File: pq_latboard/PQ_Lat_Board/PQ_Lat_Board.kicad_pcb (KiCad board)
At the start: 6 copper layers, 48 x 48 mm, 20 parts, among them IC1 TCN75AVOA713, J1 Conn_01x11_MountingPin, J2 connector-coax

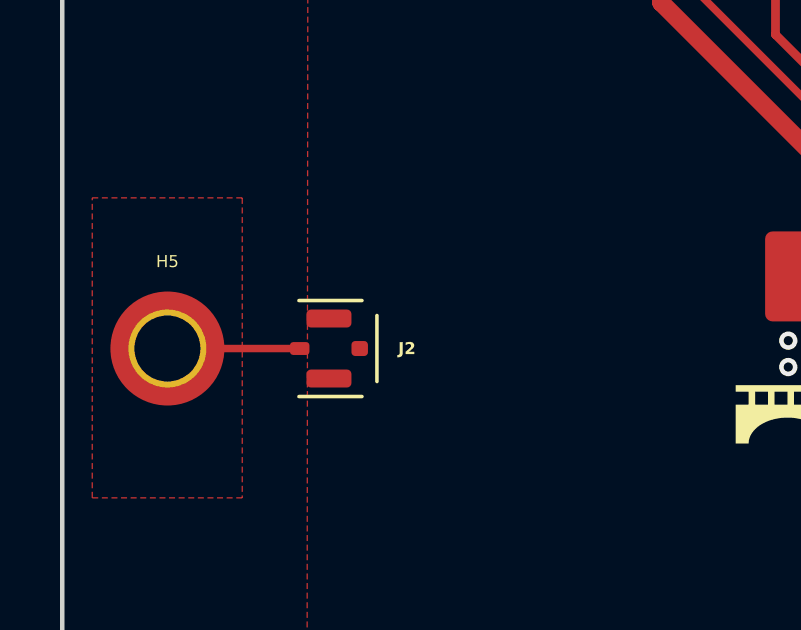
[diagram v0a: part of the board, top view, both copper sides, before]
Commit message: solved wrong connector in lateral board
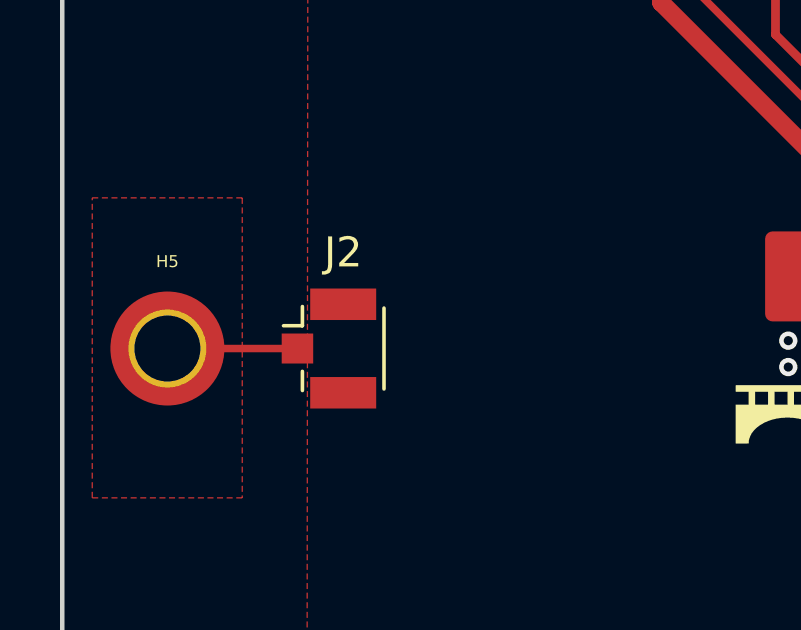
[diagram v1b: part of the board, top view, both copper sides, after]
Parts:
- J2: value connector-coax -> Conn_Coaxial; footprint -nsl_connector:C.FL-R-SMT-1(90) -> Connector_Coaxial:U.FL_Hirose_U.FL-R-SMT-1_Vertical
- turned J2 to 0 degrees
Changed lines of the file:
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@@
       (net 8 "/Antenna Connector") (pinfunction "1") (pintype "input"))
   )
-  (footprint "-nsl_connector:C.FL-R-SMT-1(90)" (layer "F.Cu")
-    (at 83.89 66.0224 -90)
-    (property "Manufacturer 1" "Hirose")
-    (property "Manufacturer Part Number 1" "C.FL-R-SMT-1")
+  (footprint "Connector_Coaxial:U.FL_Hirose_U.FL-R-SMT-1_Vertical" (layer "F.Cu")
+    (at 83.89 66.0224)
+    (descr "Hirose U.FL Coaxial https://www.hirose.com/product/en/products/U.FL/U.FL-R-SMT-1%2810%29/")
+    (tags "Hirose U.FL Coaxial")
     (property "Sheetfile" "PQ_Lat_Board.kicad_sch")
     (property "Sheetname" "")
-    (property "Supplier 1" "Mouser")
-    (property "Supplier Part Number 1" "798-CFL-R-SMT-190 ")
+    (property "ki_description" "coaxial connector (BNC, SMA, SMB, SMC, Cinch/RCA, LEMO, ...)")
+    (property "ki_keywords" "BNC SMA SMB SMC LEMO coaxial connector CINCH RCA")
     (attr smd)
-    (fp_text reference "J2" (at 0 -2.6 unlocked) (layer "F.SilkS")
-        (effects (font (size 0.4 0.4) (thickness 0.1) bold))
-    )
-    (fp_text value "connector-coax" (at 0 -5.4 -90 unlocked) (layer "F.Fab")
+    (fp_text reference "J2" (at 0.475 -3.2) (layer "F.SilkS")
         (effects (font (size 1 1) (thickness 0.15)))
     )
-    (fp_text user "${REFERENCE}" (at 0 -3.9 -90 unlocked) (layer "F.Fab")
+    (fp_text value "Conn_Coaxial" (at 0.475 3.2) (layer "F.Fab")
         (effects (font (size 1 1) (thickness 0.15)))
     )
-    (fp_line (start -1.6 1) (end -1.6 -1.1)
+    (fp_text user "${REFERENCE}" (at 0.475 0 90) (layer "F.Fab")
+        (effects (font (size 0.6 0.6) (thickness 0.09)))
+    )
+    (fp_line (start -0.885 -1.4) (end -0.885 -0.76)
       (stroke (width 0.12) (type solid)) (layer "F.SilkS"))
-    (fp_line (start -1.1 -1.6) (end 1.1 -1.6)
+    (fp_line (start -0.885 -0.76) (end -1.515 -0.76)
       (stroke (width 0.12) (type solid)) (layer "F.SilkS"))
-    (fp_line (start 1.6 -1.1) (end 1.6 1)
+    (fp_line (start -0.885 1.4) (end -0.885 0.76)
       (stroke (width 0.12) (type solid)) (layer "F.SilkS"))
-    (pad "1" smd roundrect (at 0 0.975 90) (size 0.43 0.65) (layers "F.Cu" "F.Paste" "F.Mask") (roundrect_rratio 0.25)
-      (net 8 "/Antenna Connector") (pintype "bidirectional"))
-    (pad "2" smd roundrect (at -1 0 90) (size 0.6 1.5) (layers "F.Cu" "F.Paste" "F.Mask") (roundrect_rratio 0.25)
-      (net 9 "GND") (pintype "bidirectional"))
-    (pad "2" smd roundrect (at 0 -1.025 90) (size 0.5 0.55) (layers "F.Cu" "F.Paste" "F.Mask") (roundrect_rratio 0.25)
-      (net 9 "GND") (pintype "bidirectional"))
-    (pad "2" smd roundrect (at 1 0 90) (size 0.6 1.5) (layers "F.Cu" "F.Paste" "F.Mask") (roundrect_rratio 0.25)
-      (net 9 "GND") (pintype "bidirectional"))
-    (model "${KICAD_NSL_DIR}/connector-nsl/StepFiles/C.FL-R-SMT-1(90).stp"
-      (offset (xyz 0 0 0))
+    (fp_line (start 1.835 -1.35) (end 1.835 1.35)
+      (stroke (width 0.12) (type solid)) (layer "F.SilkS"))
+    (fp_line (start -2.02 1) (end -2.02 -1)
+      (stroke (width 0.05) (type solid)) (layer "F.CrtYd"))
+    (fp_line (start -1.32 -1.8) (end -1.12 -1.8)
+      (stroke (width 0.05) (type solid)) (layer "F.CrtYd"))
+    (fp_line (start -1.32 -1) (end -2.02 -1)
+      (stroke (width 0.05) (type solid)) (layer "F.CrtYd"))
+    (fp_line (start -1.32 -1) (end -1.32 -1.8)
+      (stroke (width 0.05) (type solid)) (layer "F.CrtYd"))
+    (fp_line (start -1.32 1) (end -2.02 1)
+      (stroke (width 0.05) (type solid)) (layer "F.CrtYd"))
+    (fp_line (start -1.32 1.8) (end -1.32 1)
+      (stroke (width 0.05) (type solid)) (layer "F.CrtYd"))
+    (fp_line (start -1.32 1.8) (end -1.12 1.8)
+      (stroke (width 0.05) (type solid)) (layer "F.CrtYd"))
+    (fp_line (start -1.12 -1.8) (end -1.12 -2.5)
+      (stroke (width 0.05) (type solid)) (layer "F.CrtYd"))
+    (fp_line (start -1.12 2.5) (end -1.12 1.8)
+      (stroke (width 0.05) (type solid)) (layer "F.CrtYd"))
+    (fp_line (start 2.08 -2.5) (end -1.12 -2.5)
+      (stroke (width 0.05) (type solid)) (layer "F.CrtYd"))
+    (fp_line (start 2.08 -1.8) (end 2.08 -2.5)
+      (stroke (width 0.05) (type solid)) (layer "F.CrtYd"))
+    (fp_line (start 2.08 -1.8) (end 2.28 -1.8)
+      (stroke (width 0.05) (type solid)) (layer "F.CrtYd"))
+    (fp_line (start 2.08 1.8) (end 2.28 1.8)
+      (stroke (width 0.05) (type solid)) (layer "F.CrtYd"))
+    (fp_line (start 2.08 2.5) (end -1.12 2.5)
+      (stroke (width 0.05) (type solid)) (layer "F.CrtYd"))
+    (fp_line (start 2.08 2.5) (end 2.08 1.8)
+      (stroke (width 0.05) (type solid)) (layer "F.CrtYd"))
+    (fp_line (start 2.28 1.8) (end 2.28 -1.8)
+      (stroke (width 0.05) (type solid)) (layer "F.CrtYd"))
+    (fp_line (start -1.075 0.3) (end -1.075 -0.15)
+      (stroke (width 0.1) (type solid)) (layer "F.Fab"))
+    (fp_line (start -1.075 0.3) (end -0.825 0.3)
+      (stroke (width 0.1) (type solid)) (layer "F.Fab"))
+    (fp_line (start -0.925 -0.3) (end -1.075 -0.15)
+      (stroke (width 0.1) (type solid)) (layer "F.Fab"))
+    (fp_line (start -0.925 -0.3) (end -0.825 -0.3)
+      (stroke (width 0.1) (type solid)) (layer "F.Fab"))
+    (fp_line (start -0.825 -0.3) (end -0.825 -1.3)
+      (stroke (width 0.1) (type solid)) (layer "F.Fab"))
+    (fp_line (start -0.825 0.3) (end -0.825 1.3)
+      (stroke (width 0.1) (type solid)) (layer "F.Fab"))
+    (fp_line (start -0.425 -1.5) (end -0.425 -1.3)
+      (stroke (width 0.1) (type solid)) (layer "F.Fab"))
+    (fp_line (start -0.425 -1.5) (end 1.375 -1.5)
+      (stroke (width 0.1) (type solid)) (layer "F.Fab"))
+    (fp_line (start -0.425 -1.3) (end -0.825 -1.3)
+      (stroke (width 0.1) (type solid)) (layer "F.Fab"))
+    (fp_line (start -0.425 1.3) (end -0.825 1.3)
+      (stroke (width 0.1) (type solid)) (layer "F.Fab"))
+    (fp_line (start -0.425 1.5) (end -0.425 1.3)
+      (stroke (width 0.1) (type solid)) (layer "F.Fab"))
+    (fp_line (start -0.425 1.5) (end 1.375 1.5)
+      (stroke (width 0.1) (type solid)) (layer "F.Fab"))
+    (fp_line (start 1.375 -1.5) (end 1.375 -1.3)
+      (stroke (width 0.1) (type solid)) (layer "F.Fab"))
+    (fp_line (start 1.375 1.5) (end 1.375 1.3)
+      (stroke (width 0.1) (type solid)) (layer "F.Fab"))
+    (fp_line (start 1.775 -1.3) (end 1.375 -1.3)
+      (stroke (width 0.1) (type solid)) (layer "F.Fab"))
+    (fp_line (start 1.775 -1.3) (end 1.775 1.3)
+      (stroke (width 0.1) (type solid)) (layer "F.Fab"))
+    (fp_line (start 1.775 1.3) (end 1.375 1.3)
+      (stroke (width 0.1) (type solid)) (layer "F.Fab"))
+    (pad "1" smd rect (at -1.05 0) (size 1.05 1) (layers "F.Cu" "F.Paste" "F.Mask")
+      (net 8 "/Antenna Connector") (pinfunction "In") (pintype "passive"))
+    (pad "2" smd rect (at 0.475 -1.475) (size 2.2 1.05) (layers "F.Cu" "F.Paste" "F.Mask")
+      (net 9 "GND") (pinfunction "Ext") (pintype "passive"))
+    (pad "2" smd rect (at 0.475 1.475) (size 2.2 1.05) (layers "F.Cu" "F.Paste" "F.Mask")
+      (net 9 "GND") (pinfunction "Ext") (pintype "passive"))
+    (model "${KICAD6_3DMODEL_DIR}/Connector_Coaxial.3dshapes/U.FL_Hirose_U.FL-R-SMT-1_Vertical.wrl"
+      (offset (xyz 0.4749999928 0 0))
       (scale (xyz 1 1 1))
       (rotate (xyz 0 0 0))

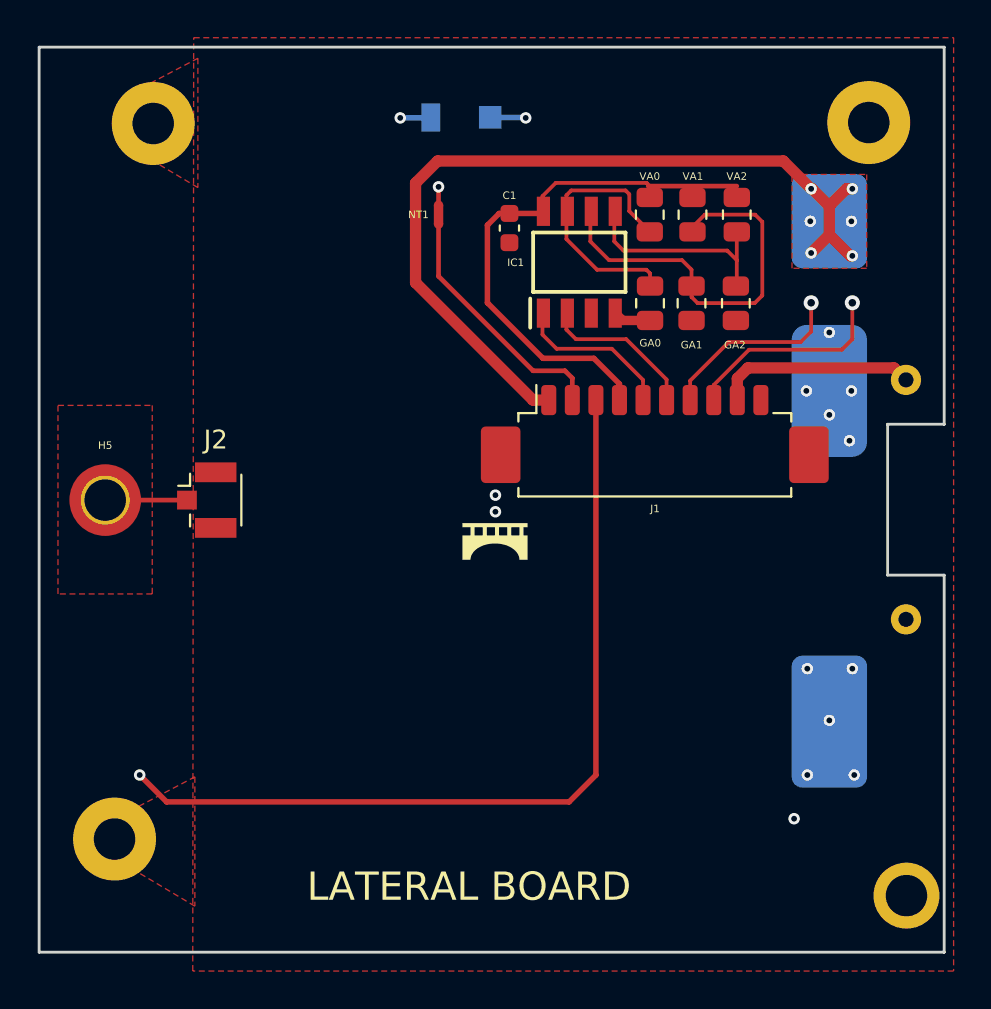
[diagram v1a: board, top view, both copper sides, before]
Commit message: add names, bigger hole and mirror solar cell
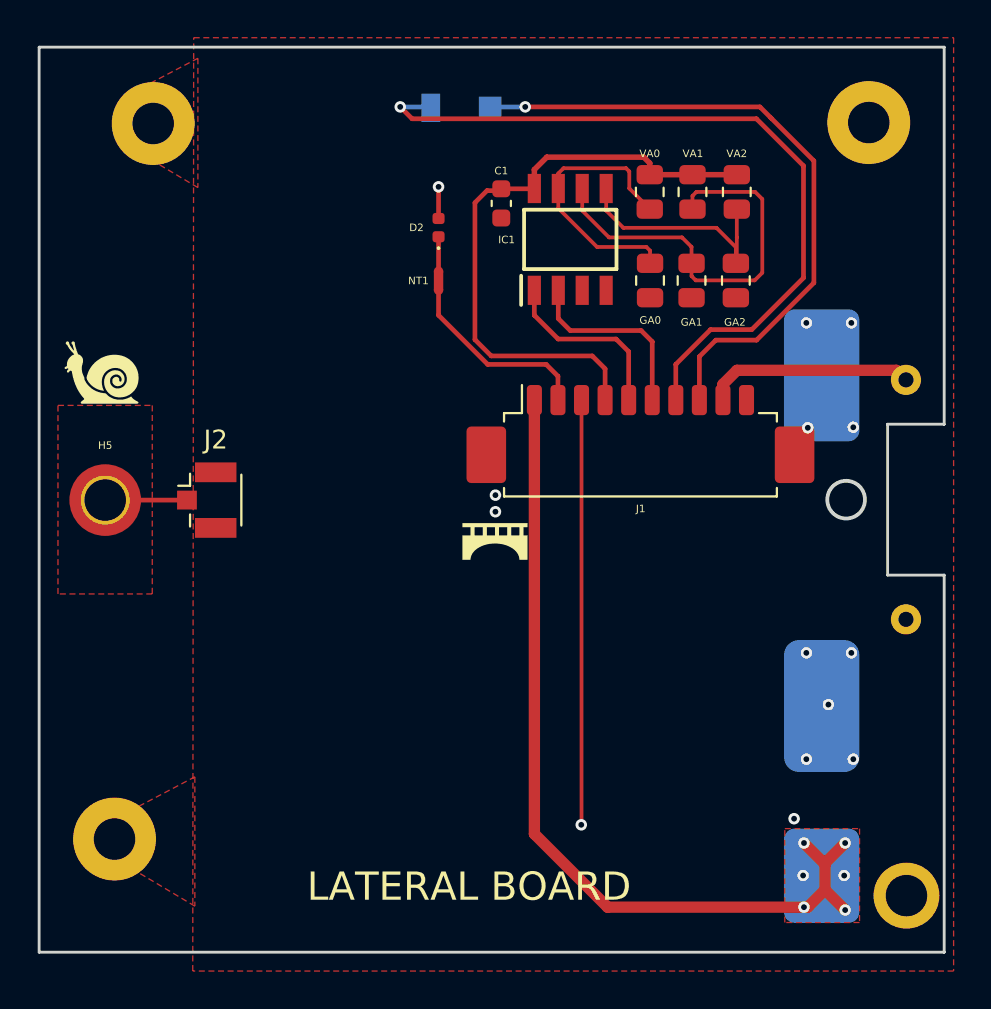
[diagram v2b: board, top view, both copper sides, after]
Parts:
- added Annotation2: Silkscreen_Annotation, symbols-nsl:snail, F.Cu at (78.3, 59.3)
- added Annotation3: LOGO, symbols-nsl:pocat-lektron, B.Cu at (108.9, 45.1)
- added Annotation4: Logo lektron, symbols-nsl:logo_pq, B.Cu at (78.8, 57.0)
- added Annotation5: telecos, symbols-nsl:Telecos, B.Cu at (88.5, 45.3)
- added Annotation6: telecos, symbols-nsl:NSL-small, B.Cu at (76.9, 75.0)
- added Annotation7: IEEE, symbols-nsl:UPC_small, B.Cu at (80.3, 72.9)
- added Annotation8: GRSS, symbols-nsl:GRSS, B.Cu at (118.3, 52.1)
- added D2: LED, LED_SMD:LED_0402_1005Metric, F.Cu at (96.2, 51.6)
- moved NT1 3.51 mm to (96.2, 54.4)
- moved C1 1.38 mm to (99.5, 50.3)
- moved IC1 1.30 mm to (103.1, 52.2)
- moved VA0 1.21 mm to (107.4, 49.7)
- moved VA1 1.21 mm to (109.7, 49.7)
- moved VA2 1.21 mm to (112.0, 49.7)
- moved GA0 1.21 mm to (107.4, 54.4)
- moved GA1 1.21 mm to (109.6, 54.4)
- moved GA2 1.21 mm to (112.0, 54.4)
- moved J1 0.76 mm to (106.9, 63.1)
- moved D1 0.51 mm to (97.7, 45.3)
- moved SC1 0.41 mm to (113.5, 88.9)
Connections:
- NT1 pad 1: /VCC_MAG -> Net-(D2-K)
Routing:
- net /VCC: track 28.6 -> 32.6 mm
- net /VCC_MAG: track 9698.0 -> 9694.4 mm
- net /PH+: track 37.9 -> 34.8 mm, vias 2 -> 1
- net /ADCS: track 13.3 -> 10.3 mm
- net /SOLAR: track 44.5 -> 46.4 mm
- net GND: track 1.88 -> 0.00 mm, vias 10 -> 9
- net Net-(D2-K): track 0.00 -> 1.83 mm
- net /SCL: track 8.43 -> 10.1 mm
- net /PH-: track 42.4 -> 40.8 mm, vias 2 -> 1
- net Net-(IC1-A2): track 11.4 -> 12.7 mm
- net /SDA: track 8.59 -> 9.69 mm
- net Net-(IC1-A1): track 21.3 -> 21.9 mm
- net Net-(IC1-A0): track 14.2 -> 14.7 mm
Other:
- outline, holes or cut-outs redrawn
- board text added: "Roger Almirall Júlia Alós Adriano Camps Marc Corretgé Artur Cot Arnau Dolz Vladimir Frunză Edgar Hernandez Óscar Pavón Ştefan Podaru"

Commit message: Removed netie, updated SC footprint, trace reform, logo&name cleanup, footprint reconciled, DRC
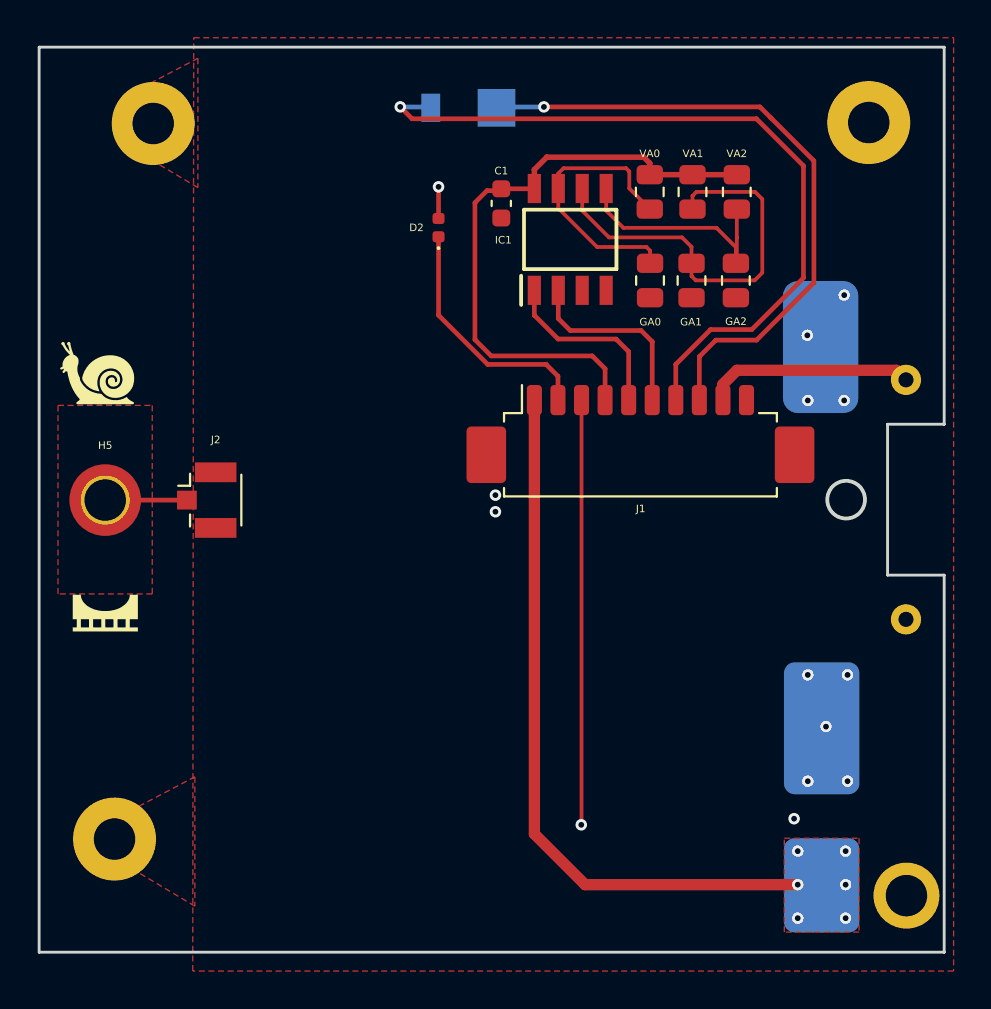
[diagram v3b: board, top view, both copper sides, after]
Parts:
- removed NT1: NetTie_2, NetTie:NetTie-2_SMD_Pad0.5mm
- Annotation1: value Silkscreen_Annotation -> bridgemaker; footprint -nsl_symbols:Bridgemaker -> symbols-nsl:Bridgemaker
- Annotation2: value Silkscreen_Annotation -> Snail; footprint symbols-nsl:snail -> symbols-nsl:Snail
- Annotation3: value LOGO -> pocat_lektron; footprint symbols-nsl:pocat-lektron -> symbols-nsl:pocat_lektron
- Annotation4: footprint symbols-nsl:logo_pq -> symbols-nsl:NSL_hexagon
- Annotation6: value telecos -> Nanosatlab
- Annotation7: value IEEE -> UPC
- D1: footprint -nsl_passive:SLCD-61N8 -> passive-nsl:SLCD-61N8
- IC1: footprint -nsl_sensor:TCN75AVOA -> sensor-nsl:TCN75AVOA
- moved Annotation3 41.3 mm to (79.8, 74.4), turned to 90 degrees
- moved Annotation8 40.3 mm to (78.8, 60.0), turned to 90 degrees
- moved Annotation7 39.6 mm to (108.5, 45.2), turned to 180 degrees
- moved Annotation1 20.9 mm to (78.6, 71.9), turned to 180 degrees
- moved Annotation4 5.44 mm to (78.8, 51.5)
- moved Annotation2 0.68 mm to (78.8, 59.7)
- moved Annotation6 0.58 mm to (77.4, 74.8)
- moved Annotation5 0.15 mm to (88.5, 45.1)
- turned GA0 to -90 degrees
- turned GA1 to -90 degrees
- turned GA2 to -90 degrees
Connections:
- D2 pad 1: Net-(D2-K) -> /ADCS
- GA0 pad 1: GND -> Net-(IC1-A0)
- GA0 pad 2: Net-(IC1-A0) -> GND
- GA1 pad 1: GND -> Net-(IC1-A1)
- GA1 pad 2: Net-(IC1-A1) -> GND
- GA2 pad 1: GND -> Net-(IC1-A2)
- GA2 pad 2: Net-(IC1-A2) -> GND
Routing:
- net /SOLAR: track 46.4 -> 38.1 mm
- net /ADCS: track 10.3 -> 13.1 mm
- net Net-(D2-K): track 1.83 -> 0.00 mm
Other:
- board text added: "Adriano Camps Ştefan Podaru Guillem Gràcia Solá Marc Corretgé Artur Cot Arnau Dolz Edgar Hernández Roger Almirall Júlia Alós Óscar Pavón Nil Rius Júlia Tribó"
- board text removed: "D1"
- board text removed: "LATERAL BOARD"
- board text removed: "Roger Almirall Júlia Alós Adriano Camps Marc Corretgé Artur Cot Arnau Dolz Vladimir Frunză Edgar Hernandez Óscar Pavón Ştefan Podaru"
